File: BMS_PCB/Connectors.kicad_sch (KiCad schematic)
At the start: 6 parts, among them J1 Conn_01x37

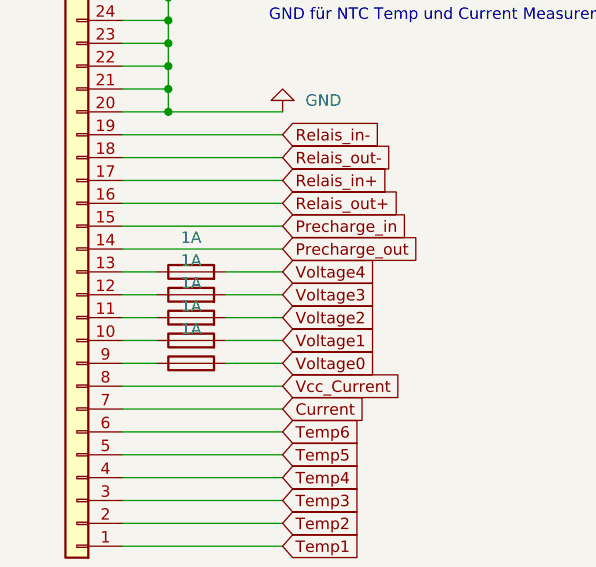
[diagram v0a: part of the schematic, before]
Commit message: Changes Schematic
- Symbol Relais
- add DUMMY
- changed Fuses 100mA
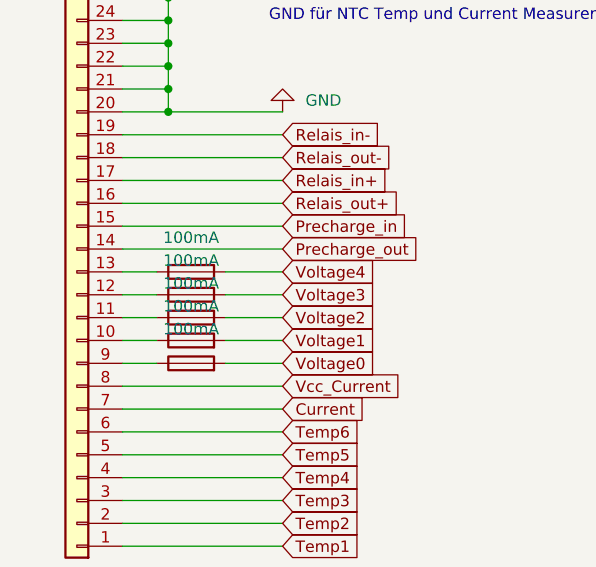
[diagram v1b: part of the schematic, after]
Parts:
- F1, F2, F3, F4, F6: value 1A -> 100mA; footprint Fuse:Fuseholder_Littelfuse_Nano2_154x -> Fuse:Fuse_Littelfuse-NANO2-451_453
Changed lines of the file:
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@@
 			)
 		)
-		(property "Value" "1A"
+		(property "Value" "100mA"
 			(at 44.45 116.84 90)
 			(effects
@@
 			)
 		)
-		(property "Footprint" "Fuse:Fuseholder_Littelfuse_Nano2_154x"
+		(property "Footprint" "Fuse:Fuse_Littelfuse-NANO2-451_453"
 			(at 44.45 122.428 90)
 			(effects
@@
 			)
 		)
-		(property "Value" "1A"
+		(property "Value" "100mA"
 			(at 44.45 114.3 90)
 			(effects
@@
 			)
 		)
-		(property "Footprint" "Fuse:Fuseholder_Littelfuse_Nano2_154x"
+		(property "Footprint" "Fuse:Fuse_Littelfuse-NANO2-451_453"
 			(at 44.45 119.888 90)
 			(effects
@@
 			)
 		)
-		(property "Value" "1A"
+		(property "Value" "100mA"
 			(at 44.45 121.92 90)
 			(effects
@@
 			)
 		)
-		(property "Footprint" "Fuse:Fuseholder_Littelfuse_Nano2_154x"
+		(property "Footprint" "Fuse:Fuse_Littelfuse-NANO2-451_453"
 			(at 44.45 127.508 90)
 			(effects
@@
 			)
 		)
-		(property "Value" "1A"
+		(property "Value" "100mA"
 			(at 44.45 119.38 90)
 			(effects
@@
 			)
 		)
-		(property "Footprint" "Fuse:Fuseholder_Littelfuse_Nano2_154x"
+		(property "Footprint" "Fuse:Fuse_Littelfuse-NANO2-451_453"
 			(at 44.45 124.968 90)
 			(effects
@@
 			)
 		)
-		(property "Value" "1A"
+		(property "Value" "100mA"
 			(at 44.45 111.76 90)
 			(effects
@@
 			)
 		)
-		(property "Footprint" "Fuse:Fuseholder_Littelfuse_Nano2_154x"
+		(property "Footprint" "Fuse:Fuse_Littelfuse-NANO2-451_453"
 			(at 44.45 117.348 90)
 			(effects

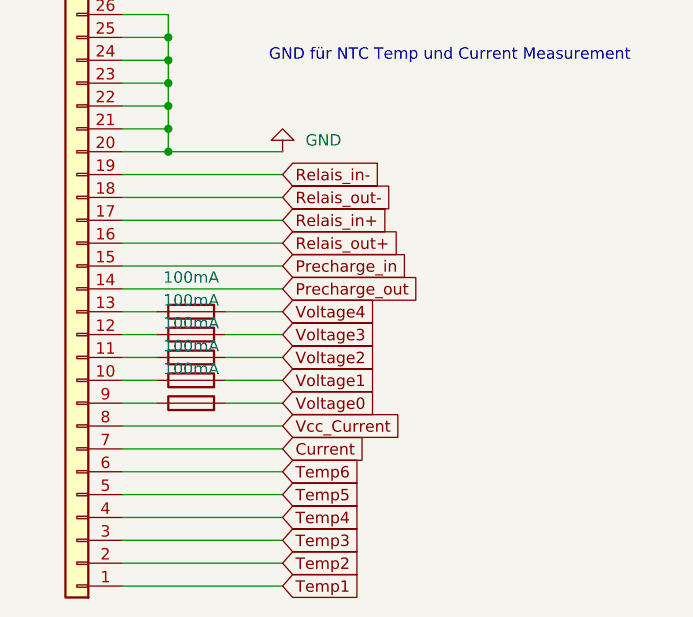
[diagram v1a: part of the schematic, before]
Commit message: Connector
Ich hab die Pinbelegung vom DSUB Stecker in Schematics geändert
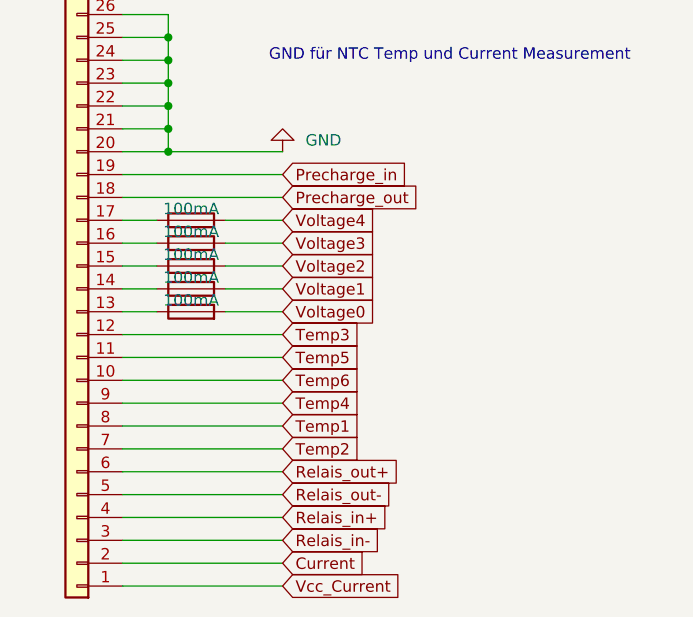
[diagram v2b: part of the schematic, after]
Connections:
- net Current: now also J1.2 (Pin_2); no longer J1.7 (Pin_7)
- net Precharge_in: now also J1.19 (Pin_19); no longer J1.15 (Pin_15)
- net Precharge_out: now also J1.18 (Pin_18); no longer J1.14 (Pin_14)
- net Relais_in+: now also J1.4 (Pin_4); no longer J1.17 (Pin_17)
- net Relais_in-: now also J1.3 (Pin_3); no longer J1.19 (Pin_19)
- net Relais_out+: now also J1.6 (Pin_6); no longer J1.16 (Pin_16)
- net Relais_out-: now also J1.5 (Pin_5); no longer J1.18 (Pin_18)
- net Temp1: now also J1.8 (Pin_8); no longer J1.1 (Pin_1)
- net Temp2: now also J1.7 (Pin_7); no longer J1.2 (Pin_2)
- net Temp3: now also J1.12 (Pin_12); no longer J1.3 (Pin_3)
- net Temp4: now also J1.9 (Pin_9); no longer J1.4 (Pin_4)
- net Temp5: now also J1.11 (Pin_11); no longer J1.5 (Pin_5)
- net Temp6: now also J1.10 (Pin_10); no longer J1.6 (Pin_6)
- net Vcc_Current: now also J1.1 (Pin_1); no longer J1.8 (Pin_8)
- net at F3.1: now also J1.15 (Pin_15); no longer J1.11 (Pin_11)
- net at F2.1: now also J1.16 (Pin_16); no longer J1.12 (Pin_12)
- net at F4.1: now also J1.14 (Pin_14); no longer J1.10 (Pin_10)
- net at J1.13 (Pin_13): now also F6.1; no longer F1.1
- new net: F1.1, J1.17 (Pin_17)

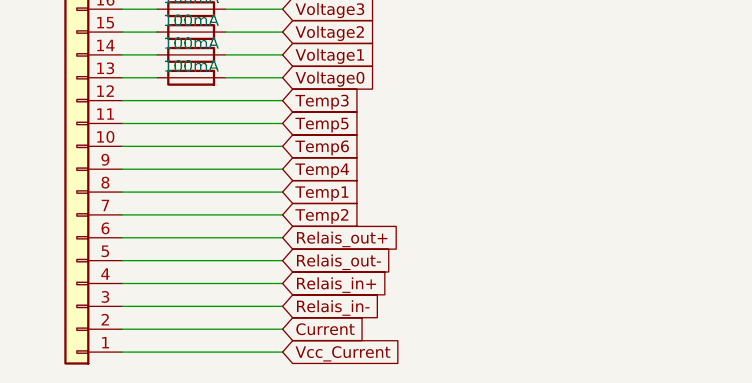
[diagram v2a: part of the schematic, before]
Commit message: kleine Änderungen
Grounding angepasst
Connector angepasst
Beschriftung angepasst
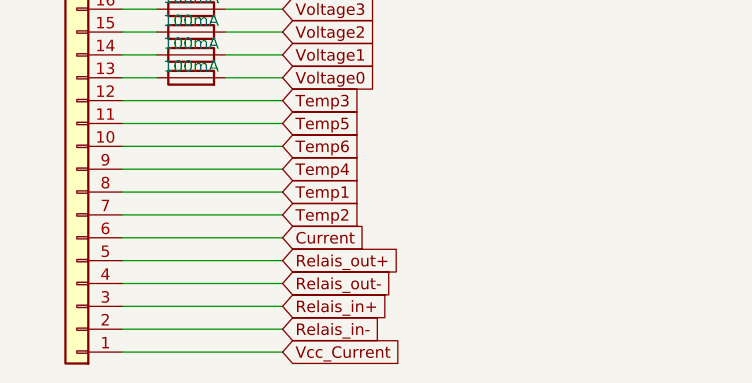
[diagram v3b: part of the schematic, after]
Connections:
- net Current: now also J1.6 (Pin_6); no longer J1.2 (Pin_2)
- net Relais_in+: now also J1.3 (Pin_3); no longer J1.4 (Pin_4)
- net Relais_in-: now also J1.2 (Pin_2); no longer J1.3 (Pin_3)
- net Relais_out+: now also J1.5 (Pin_5); no longer J1.6 (Pin_6)
- net Relais_out-: now also J1.4 (Pin_4); no longer J1.5 (Pin_5)

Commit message: Bugfixes
noch ein paar Fehler ausgemerzt
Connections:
- net Relais_out+: now also J1.4 (Pin_4); no longer J1.5 (Pin_5)
- net Relais_out-: now also J1.5 (Pin_5); no longer J1.4 (Pin_4)
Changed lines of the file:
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@@
+	(wire
+		(pts
+			(xy 41.91 85.09) (xy 41.91 87.63)
+		)
+		(stroke
+			(width 0)
+			(type default)
+		)
+	)
+	(wire
+		(pts
+			(xy 36.83 97.79) (xy 41.91 97.79)
+		)
+		(stroke
+			(width 0)
+			(type default)
+		)
+	)
+	(wire
+		(pts
+			(xy 36.83 105.41) (xy 40.64 105.41)
+		)
+		(stroke
+			(width 0)
+			(type default)
+		)
+	)
+	(wire
+		(pts
+			(xy 36.83 138.43) (xy 54.61 138.43)
+		)
+		(stroke
+			(width 0)
+			(type default)
+		)
+	)
+	(wire
+		(pts
+			(xy 36.83 113.03) (xy 40.64 113.03)
+		)
+		(stroke
+			(width 0)
+			(type default)
+		)
+	)
+	(wire
+		(pts
+			(xy 36.83 107.95) (xy 40.64 107.95)
+		)
+		(stroke
+			(width 0)
+			(type default)
+		)
+	)
+	(wire
+		(pts
+			(xy 48.26 113.03) (xy 54.61 113.03)
+		)
+		(stroke
+			(width 0)
+			(type default)
+		)
+	)
+	(wire
+		(pts
+			(xy 36.83 54.61) (xy 39.37 54.61)
+		)
+		(stroke
+			(width 0)
+			(type default)
+		)
+	)
+	(wire
+		(pts
+			(xy 36.83 57.15) (xy 39.37 57.15)
+		)
+		(stroke
+			(width 0)
+			(type default)
+		)
+	)
+	(wire
+		(pts
+			(xy 41.91 92.71) (xy 41.91 95.25)
+		)
+		(stroke
+			(width 0)
+			(type default)
+		)
+	)
+	(wire
+		(pts
+			(xy 36.83 87.63) (xy 41.91 87.63)
+		)
+		(stroke
+			(width 0)
+			(type default)
+		)
+	)
+	(wire
+		(pts
+			(xy 48.26 115.57) (xy 54.61 115.57)
+		)
+		(stroke
+			(width 0)
+			(type default)
+		)
+	)
 	(wire
 		(pts
@@
 	(wire
 		(pts
-			(xy 41.91 85.09) (xy 41.91 87.63)
-		)
-		(stroke
-			(width 0)
-			(type default)
-		)
-	)
-	(wire
-		(pts
-			(xy 36.83 97.79) (xy 41.91 97.79)
-		)
-		(stroke
-			(width 0)
-			(type default)
-		)
-	)
-	(wire
-		(pts
-			(xy 36.83 105.41) (xy 40.64 105.41)
-		)
-		(stroke
-			(width 0)
-			(type default)
-		)
-	)
-	(wire
-		(pts
-			(xy 36.83 113.03) (xy 40.64 113.03)
-		)
-		(stroke
-			(width 0)
-			(type default)
-		)
-	)
-	(wire
-		(pts
-			(xy 36.83 107.95) (xy 40.64 107.95)
-		)
-		(stroke
-			(width 0)
-			(type default)
-		)
-	)
-	(wire
-		(pts
-			(xy 48.26 113.03) (xy 54.61 113.03)
-		)
-		(stroke
-			(width 0)
-			(type default)
-		)
-	)
-	(wire
-		(pts
-			(xy 36.83 54.61) (xy 39.37 54.61)
-		)
-		(stroke
-			(width 0)
-			(type default)
-		)
-	)
-	(wire
-		(pts
-			(xy 36.83 57.15) (xy 39.37 57.15)
-		)
-		(stroke
-			(width 0)
-			(type default)
-		)
-	)
-	(wire
-		(pts
-			(xy 41.91 92.71) (xy 41.91 95.25)
-		)
-		(stroke
-			(width 0)
-			(type default)
-		)
-	)
-	(wire
-		(pts
-			(xy 36.83 87.63) (xy 41.91 87.63)
-		)
-		(stroke
-			(width 0)
-			(type default)
-		)
-	)
-	(wire
-		(pts
-			(xy 48.26 115.57) (xy 54.61 115.57)
-		)
-		(stroke
-			(width 0)
-			(type default)
-		)
-	)
-	(wire
-		(pts
 			(xy 48.26 110.49) (xy 54.61 110.49)
 		)
@@
 	(wire
 		(pts
-			(xy 36.83 138.43) (xy 54.61 138.43)
-		)
-		(stroke
-			(width 0)
-			(type default)
-		)
-	)
-	(wire
-		(pts
 			(xy 36.83 128.27) (xy 54.61 128.27)
 		)
@@
 	(global_label "Relais_out-"
 		(shape input)
+		(at 54.61 135.89 0)
+		(fields_autoplaced yes)
+		(effects
+			(font
+				(size 1.27 1.27)
+			)
+			(justify left)
+		)
+		(property "Intersheetrefs" "${INTERSHEET_REFS}"
+			(at 68.9646 135.89 0)
+			(effects
+				(font
+					(size 1.27 1.27)
+				)
+				(justify left)
+				(hide yes)
+			)
+		)
+	)
+	(global_label "Temp6"
+		(shape input)
+		(at 54.61 123.19 0)
+		(fields_autoplaced yes)
+		(effects
+			(font
+				(size 1.27 1.27)
+			)
+			(justify left)
+		)
+		(property "Intersheetrefs" "${INTERSHEET_REFS}"
+			(at 63.7032 123.19 0)
+			(effects
+				(font
+					(size 1.27 1.27)
+				)
+				(justify left)
+				(hide yes)
+			)
+		)
+	)
+	(global_label "Relais_in-"
+		(shape input)
+		(at 54.61 143.51 0)
+		(fields_autoplaced yes)
+		(effects
+			(font
+				(size 1.27 1.27)
+			)
+			(justify left)
+		)
+		(property "Intersheetrefs" "${INTERSHEET_REFS}"
+			(at 67.6947 143.51 0)
+			(effects
+				(font
+					(size 1.27 1.27)
+				)
+				(justify left)
+				(hide yes)
+			)
+		)
+	)
+	(global_label "Current"
+		(shape input)
+		(at 54.61 133.35 0)
+		(fields_autoplaced yes)
+		(effects
+			(font
+				(size 1.27 1.27)
+			)
+			(justify left)
+		)
+		(property "Intersheetrefs" "${INTERSHEET_REFS}"
+			(at 64.5499 133.35 0)
+			(effects
+				(font
+					(size 1.27 1.27)
+				)
+				(justify left)
+				(hide yes)
+			)
+		)
+	)
+	(global_label "Voltage0"
+		(shape input)
+		(at 54.61 115.57 0)
+		(fields_autoplaced yes)
+		(effects
+			(font
+				(size 1.27 1.27)
+			)
+			(justify left)
+		)
+		(property "Intersheetrefs" "${INTERSHEET_REFS}"
+			(at 65.8198 115.57 0)
+			(effects
+				(font
+					(size 1.27 1.27)
+				)
+				(justify left)
+				(hide yes)
+			)
+		)
+	)
+	(global_label "Relais_out+"
+		(shape input)
 		(at 54.61 138.43 0)
 		(fields_autoplaced yes)
@@
 			(effects
 				(font
-					(size 1.27 1.27)
-				)
-				(justify left)
-				(hide yes)
-			)
-		)
-	)
-	(global_label "Temp6"
-		(shape input)
-		(at 54.61 123.19 0)
-		(fields_autoplaced yes)
-		(effects
-			(font
-				(size 1.27 1.27)
-			)
-			(justify left)
-		)
-		(property "Intersheetrefs" "${INTERSHEET_REFS}"
-			(at 63.7032 123.19 0)
-			(effects
-				(font
-					(size 1.27 1.27)
-				)
-				(justify left)
-				(hide yes)
-			)
-		)
-	)
-	(global_label "Relais_in-"
-		(shape input)
-		(at 54.61 143.51 0)
-		(fields_autoplaced yes)
-		(effects
-			(font
-				(size 1.27 1.27)
-			)
-			(justify left)
-		)
-		(property "Intersheetrefs" "${INTERSHEET_REFS}"
-			(at 67.6947 143.51 0)
-			(effects
-				(font
-					(size 1.27 1.27)
-				)
-				(justify left)
-				(hide yes)
-			)
-		)
-	)
-	(global_label "Current"
-		(shape input)
-		(at 54.61 133.35 0)
-		(fields_autoplaced yes)
-		(effects
-			(font
-				(size 1.27 1.27)
-			)
-			(justify left)
-		)
-		(property "Intersheetrefs" "${INTERSHEET_REFS}"
-			(at 64.5499 133.35 0)
-			(effects
-				(font
-					(size 1.27 1.27)
-				)
-				(justify left)
-				(hide yes)
-			)
-		)
-	)
-	(global_label "Voltage0"
-		(shape input)
-		(at 54.61 115.57 0)
-		(fields_autoplaced yes)
-		(effects
-			(font
-				(size 1.27 1.27)
-			)
-			(justify left)
-		)
-		(property "Intersheetrefs" "${INTERSHEET_REFS}"
-			(at 65.8198 115.57 0)
-			(effects
-				(font
-					(size 1.27 1.27)
-				)
-				(justify left)
-				(hide yes)
-			)
-		)
-	)
-	(global_label "Relais_out+"
-		(shape input)
-		(at 54.61 135.89 0)
-		(fields_autoplaced yes)
-		(effects
-			(font
-				(size 1.27 1.27)
-			)
-			(justify left)
-		)
-		(property "Intersheetrefs" "${INTERSHEET_REFS}"
-			(at 68.9646 135.89 0)
-			(effects
-				(font

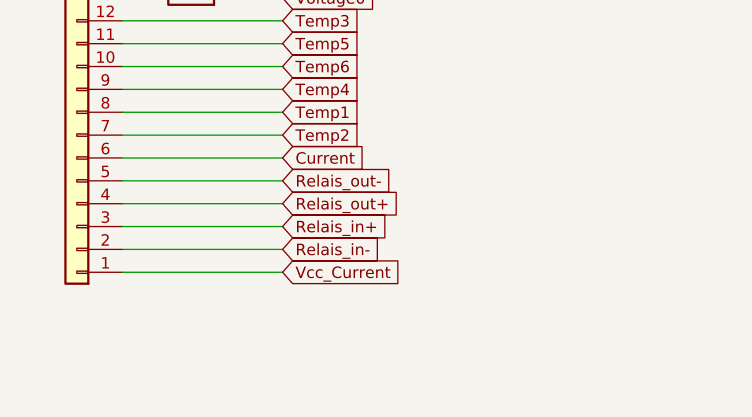
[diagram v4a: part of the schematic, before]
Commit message: changes schematic
still missing: uC pins
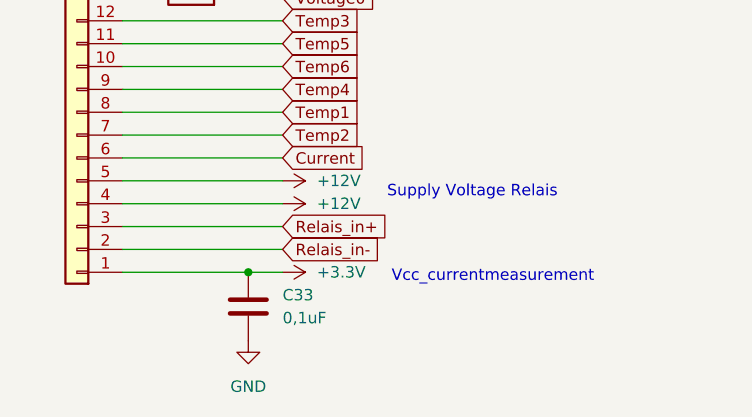
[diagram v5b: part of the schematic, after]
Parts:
- added C33: 0,1uF, Resistor_SMD:R_0603_1608Metric_Pad0.98x0.95mm_HandSolder, symbol Device:C
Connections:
- net Relais_out- is gone; now on net +12V: J1.5 (Pin_5)
- net GND: now also C33.2
- net Relais_out+ renamed +12V
- net Vcc_Current renamed +3.3V
- net +3.3V: now also C33.1
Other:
- note added: "Supply Voltage Relais"
- note added: "Vcc_currentmeasurement"

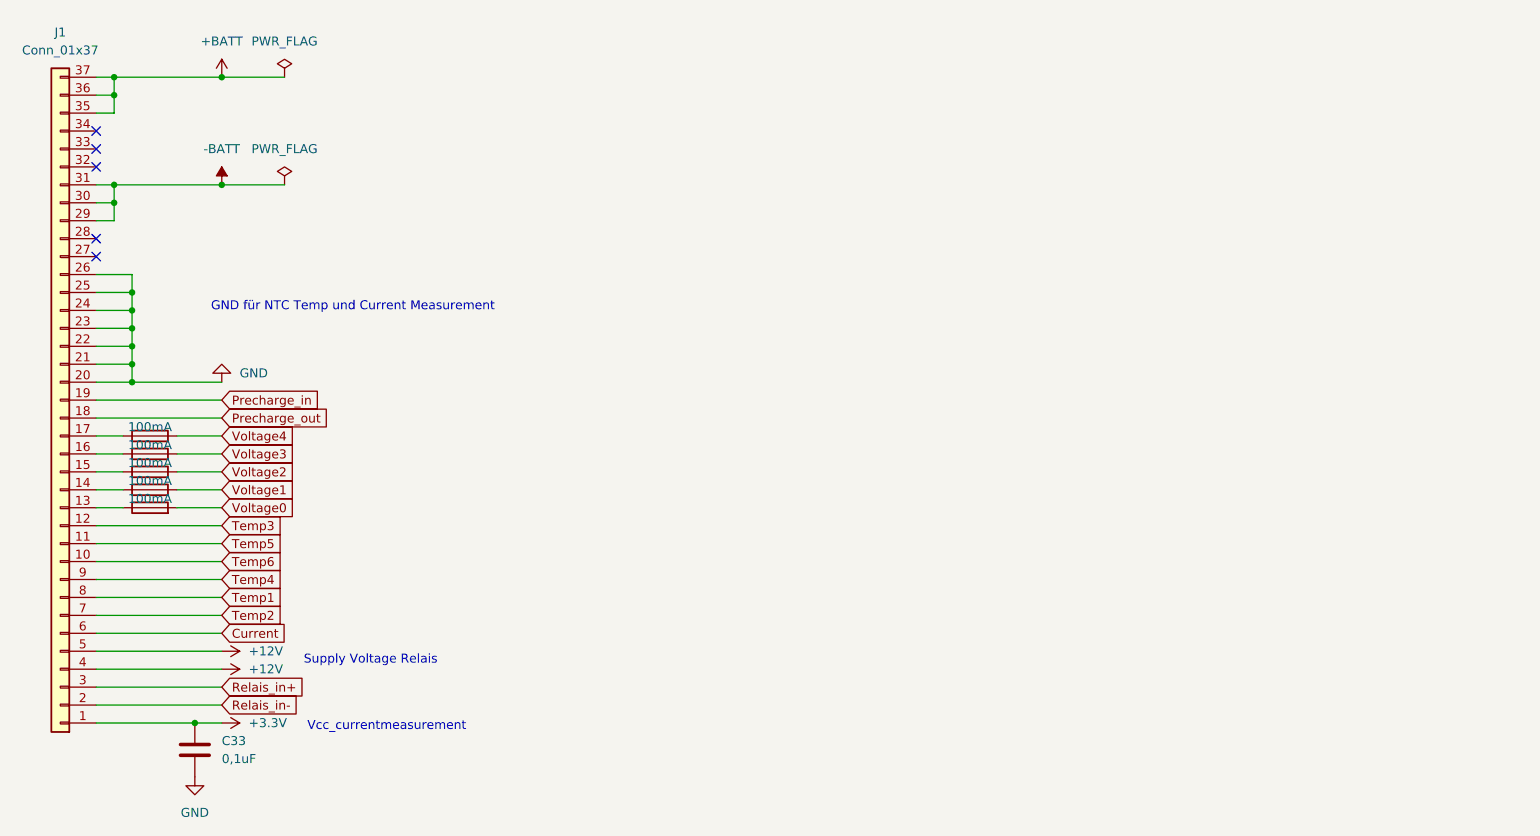
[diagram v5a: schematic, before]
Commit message: schematic uC
changes schematic uC
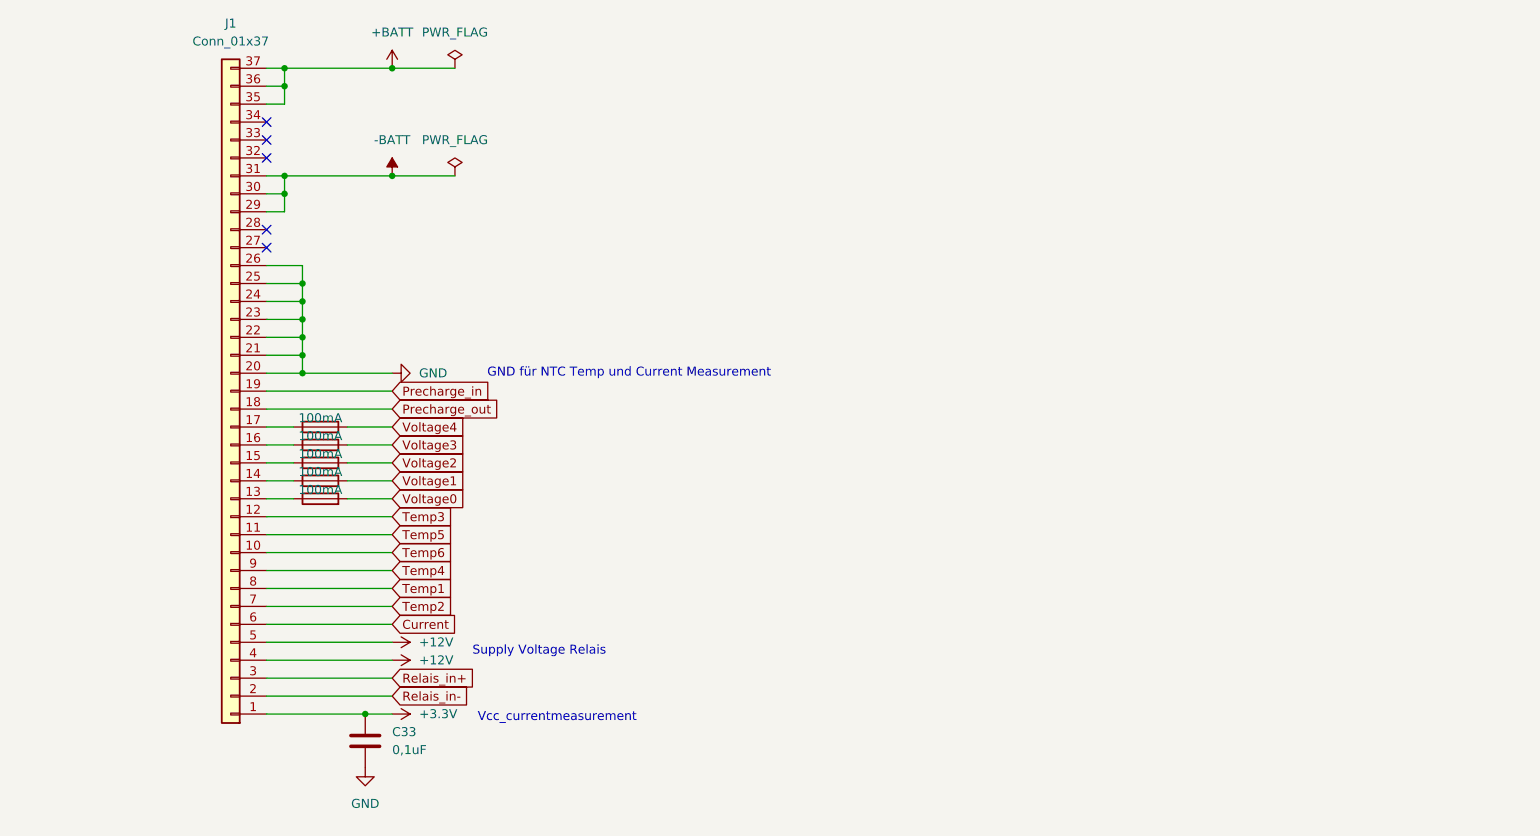
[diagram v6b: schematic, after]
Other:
- moved on the sheet: C33, J1

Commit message: Freilaufdiode
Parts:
- added D3, D4: 1N4007, Diode_SMD:D_SMA, symbol Diode:1N4007
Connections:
- net +12V: now also J1.3 (Pin_3), D3.1 (K), D4.1 (K); no longer J1.4 (Pin_4)
- net Relais_in+: now also J1.4 (Pin_4), D4.2 (A); no longer J1.3 (Pin_3)
- net Relais_in-: now also D3.2 (A)

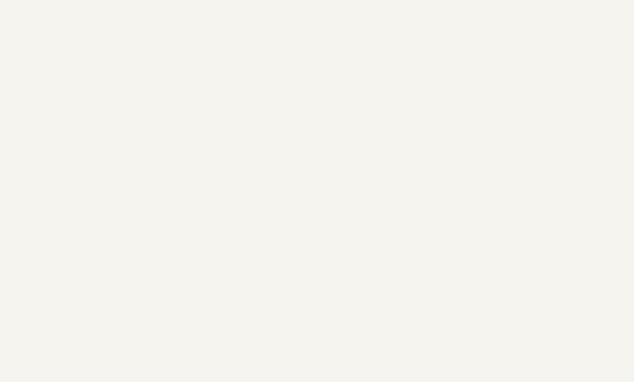
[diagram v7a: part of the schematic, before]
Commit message: Sonntag, 04.05.
Leiterbahndicken angepasst, Bohrlöcher erneuert, µC final angeschlossen, letzte Bugfixes
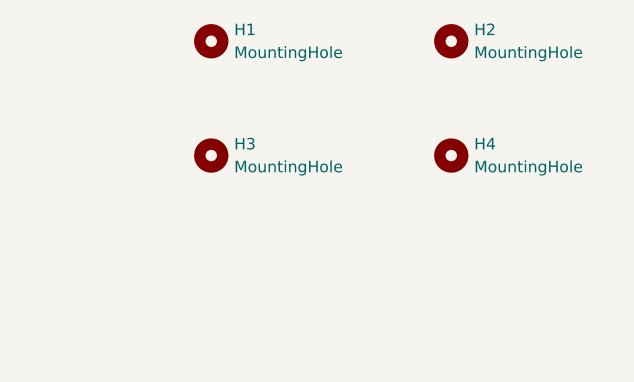
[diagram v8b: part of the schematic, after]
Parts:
- added H1, H2, H3, H4: MountingHole, MountingHole:MountingHole_3.7mm, symbol Mechanical:MountingHole
